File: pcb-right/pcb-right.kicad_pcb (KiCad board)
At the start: 2 copper layers, 143.4 x 118.9 mm, 91 parts, among them J1 Conn_01x02_Pin, J2 Conn_01x06_MountingPin, J3 Conn_01x04_Pin, SW1 SW_Push, SW2 Rotary_Encoder_Default, U1 XC6206PxxxMR, U2 STM32F401RCTx, Y1 12MHz

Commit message: moved daughter board to separate projects for left and right halves fixed layouts of daughter boards..
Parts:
- removed the R1 at (58.2, 82.7)
- removed R3: 1k, Resistor_SMD:R_0402_1005Metric
- C1, C10, C11, C12, C13, C2, C3, C4, C5, C6, C7, C8, C9: footprint Capacitor_SMD:C_0402_1005Metric -> Capacitor_SMD:C_0603_1608Metric
- R1: renamed from R5; footprint Resistor_SMD:R_0402_1005Metric -> Resistor_SMD:R_0603_1608Metric_Pad0.98x0.95mm_HandSolder
- R10, R11, R12, R13, R7, R8, R9: footprint Resistor_SMD:R_0402_1005Metric -> Resistor_SMD:R_0603_1608Metric_Pad0.98x0.95mm_HandSolder
- R2: renamed from R6; footprint Resistor_SMD:R_0402_1005Metric -> Resistor_SMD:R_0603_1608Metric_Pad0.98x0.95mm_HandSolder
- R4: renamed from R2; footprint Resistor_SMD:R_0402_1005Metric -> Resistor_SMD:R_0603_1608Metric_Pad0.98x0.95mm_HandSolder; moved to F.Cu
- R6: renamed from R4; footprint Resistor_SMD:R_0402_1005Metric -> Resistor_SMD:R_0603_1608Metric_Pad0.98x0.95mm_HandSolder; moved to F.Cu
- moved R4 18.4 mm to (62.3, 63.4), turned to -90 degrees
- moved R6 17.2 mm to (64.1, 63.4), turned to -90 degrees
- moved D29 9.23 mm to (84.9, 92.0), turned to 180 degrees
- moved R13 3.67 mm to (57.5, 86.2)
- moved R10 3.00 mm to (63.3, 90.9)
- moved R11 2.80 mm to (63.3, 95.0)
- moved J1 2.56 mm to (76.3, 86.6)
- moved R7 2.43 mm to (60.1, 86.2)
- moved C6 2.27 mm to (72.3, 81.5), turned to -90 degrees
- moved R8 2.22 mm to (60.8, 90.9)
- moved C13 2.19 mm to (69.3, 89.8)
- moved C12 2.06 mm to (72.1, 86.4)
- moved R9 1.95 mm to (60.8, 95.0)
- moved Y1 1.72 mm to (69.3, 86.4)
- moved R12 1.50 mm to (66.5, 86.4)
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- renumbered D26 to D25, D27 to D26, D28 to D27, D29 to D28, D30 to D29, MX26 to MX25, MX27 to MX26, MX28 to MX27, MX29 to MX28
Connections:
- R4 pad 2: Net-(U2-PA2) -> /UART_TX
- R6 pad 2: Net-(U2-PA3) -> /UART_RX
- U2 pad 16: Net-(U2-PA2) -> unconnected-(U2-PA2-Pad16)
- U2 pad 17: Net-(U2-PA3) -> unconnected-(U2-PA3-Pad17)
- U2 pad 37: unconnected-(U2-PC6-Pad37) -> /UART_TX
- U2 pad 38: unconnected-(U2-PC7-Pad38) -> /UART_RX
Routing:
- net /SPLIT_TX: track 38.9 -> 8.24 mm, vias 1 -> 0
- net /SPLIT_RX: track 35.3 -> 6.73 mm, vias 1 -> 0
- net /ROW4: track 154.6 -> 144.0 mm
- net /ENC_SW_2: track 3.02 -> 11.6 mm
- net +3V3: track 102.0 -> 107.3 mm
- net /UART_RX: track 0.00 -> 4.36 mm, vias 0 -> 1
- net /UART_TX: track 0.00 -> 4.36 mm, vias 0 -> 1
- net Net-(U2-PA2): track 4.20 -> 0.00 mm
- net /HANDEDNESS: track 8.20 -> 12.2 mm
- net Net-(U2-PA3): track 3.91 -> 0.00 mm
- net /ENC_B: track 13.6 -> 10.8 mm
- net /BOOTSEL: track 11.5 -> 14.2 mm
- net /ENC_A: track 14.0 -> 11.7 mm
- net /XIN: track 7.00 -> 9.21 mm
- net GND: track 19.9 -> 21.8 mm, vias 10 -> 53
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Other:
- outline, holes or cut-outs redrawn

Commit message: quick save
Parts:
- removed R1, R2: 27, Resistor_SMD:R_0603_1608Metric_Pad0.98x0.95mm_HandSolder
- removed R10, R8: 5.1k, Resistor_SMD:R_0603_1608Metric_Pad0.98x0.95mm_HandSolder
- removed R12: 1k, Resistor_SMD:R_0603_1608Metric_Pad0.98x0.95mm_HandSolder
- added C14: 100n, Capacitor_SMD:C_0603_1608Metric, B.Cu at (71.7, 45.8)
- added D30: ~, lib-zegonix:SK6812MINI-E_3.2x2.8_reverse_mount, F.Cu at (64.5, 45.8)
- added R14: 10k, Resistor_SMD:R_0603_1608Metric, B.Cu at (75.5, 111.4)
- added R15: 10k, Resistor_SMD:R_0603_1608Metric, B.Cu at (73.1, 63.5)
- C10, R4, R6, SW1: moved to B.Cu
- C12, C13: value 22p -> 12p
- J2: footprint Connector_JST:JST_SHL_SM06B-SHLS-TF_1x06-1MP_P1.00mm_Horizontal -> Connector_JST:JST_SH_SM06B-SRSS-TB_1x06-1MP_P1.00mm_Horizontal; moved to B.Cu
- R11, R9: value 5.1k -> 10K
- Y1: value 12MHz -> 8MHz
- moved SW1 66.6 mm to (58.1, 116.2)
- moved C10 53.4 mm to (59.2, 109.8), turned to 180 degrees
- moved J1 23.9 mm to (71.7, 110.1)
- moved J3 4.92 mm to (67.7, 39.0)
- moved J2 3.63 mm to (55.8, 56.6)
- moved Y1 0.62 mm to (68.8, 86.1)
- moved C13 0.49 mm to (68.8, 89.8)
- moved C12 0.38 mm to (72.1, 86.1)
- moved R4 0.25 mm to (62.0, 63.4)
- moved R6 0.25 mm to (64.3, 63.4)
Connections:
- C13 pad 2: Net-(C13-Pad2) -> /XOUT
- J1 pad 1: /BOOTSEL -> +3V3
- J1 pad 2: GND -> /BOOT0
- R11 pad 1: Net-(R10-Pad2) -> /ENC_B
- R9 pad 2: Net-(R8-Pad1) -> /ENC_A
- U2 pad 28: unconnected-(U2-PB2-Pad28) -> /BOOT1
- U2 pad 34: unconnected-(U2-PB13-Pad34) -> /IND_LED
- U2 pad 44: Net-(U2-PA11) -> /USB_D-
- U2 pad 45: Net-(U2-PA12) -> /USB_D+
- U2 pad 60: /BOOTSEL -> /BOOT0
- Y1 pad 1: Net-(C13-Pad2) -> /XOUT
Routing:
- net /BOOT0: track 0.00 -> 45.4 mm, vias 0 -> 2
- net +3V3: track 107.3 -> 148.0 mm, vias 3 -> 4
- net /IND_LED: track 0.00 -> 22.9 mm, vias 0 -> 2
- net /BOOT1: track 0.00 -> 18.9 mm, vias 0 -> 2
- net /BOOTSEL: track 14.2 -> 0.00 mm, vias 1 -> 0
- net /SWCLK: track 28.9 -> 37.2 mm
- net /USB_D-: track 13.1 -> 21.0 mm, vias 1 -> 0
- net +5V: track 6.45 -> 14.3 mm, vias 1 -> 0
- net /nRESET: track 36.9 -> 44.6 mm, vias 1 -> 2
- net /USB_D+: track 14.4 -> 22.0 mm, vias 1 -> 0
- net /SPLIT_TX: track 8.24 -> 13.5 mm
- net /SPLIT_RX: track 6.73 -> 11.8 mm
- net /XOUT: track 5.97 -> 10.7 mm
- net Net-(C13-Pad2): track 4.31 -> 0.00 mm
- net /ENC_B: track 10.8 -> 15.0 mm
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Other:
- outline, holes or cut-outs redrawn

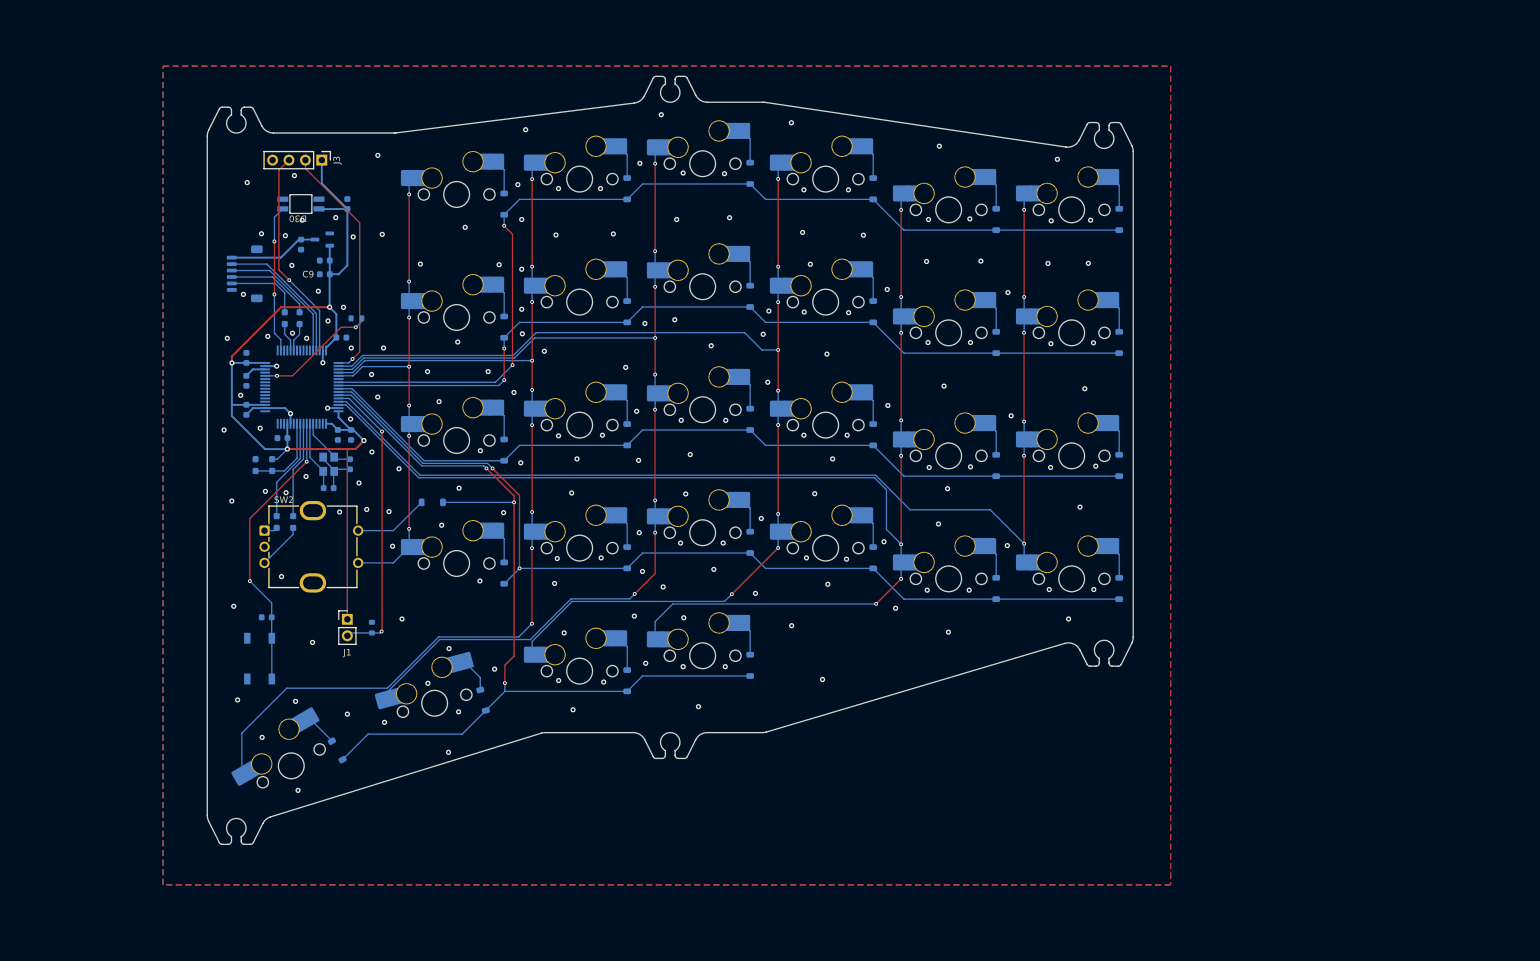
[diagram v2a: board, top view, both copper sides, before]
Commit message: finalised first version of pcbs for prototype order added openscad file for the left halfs case
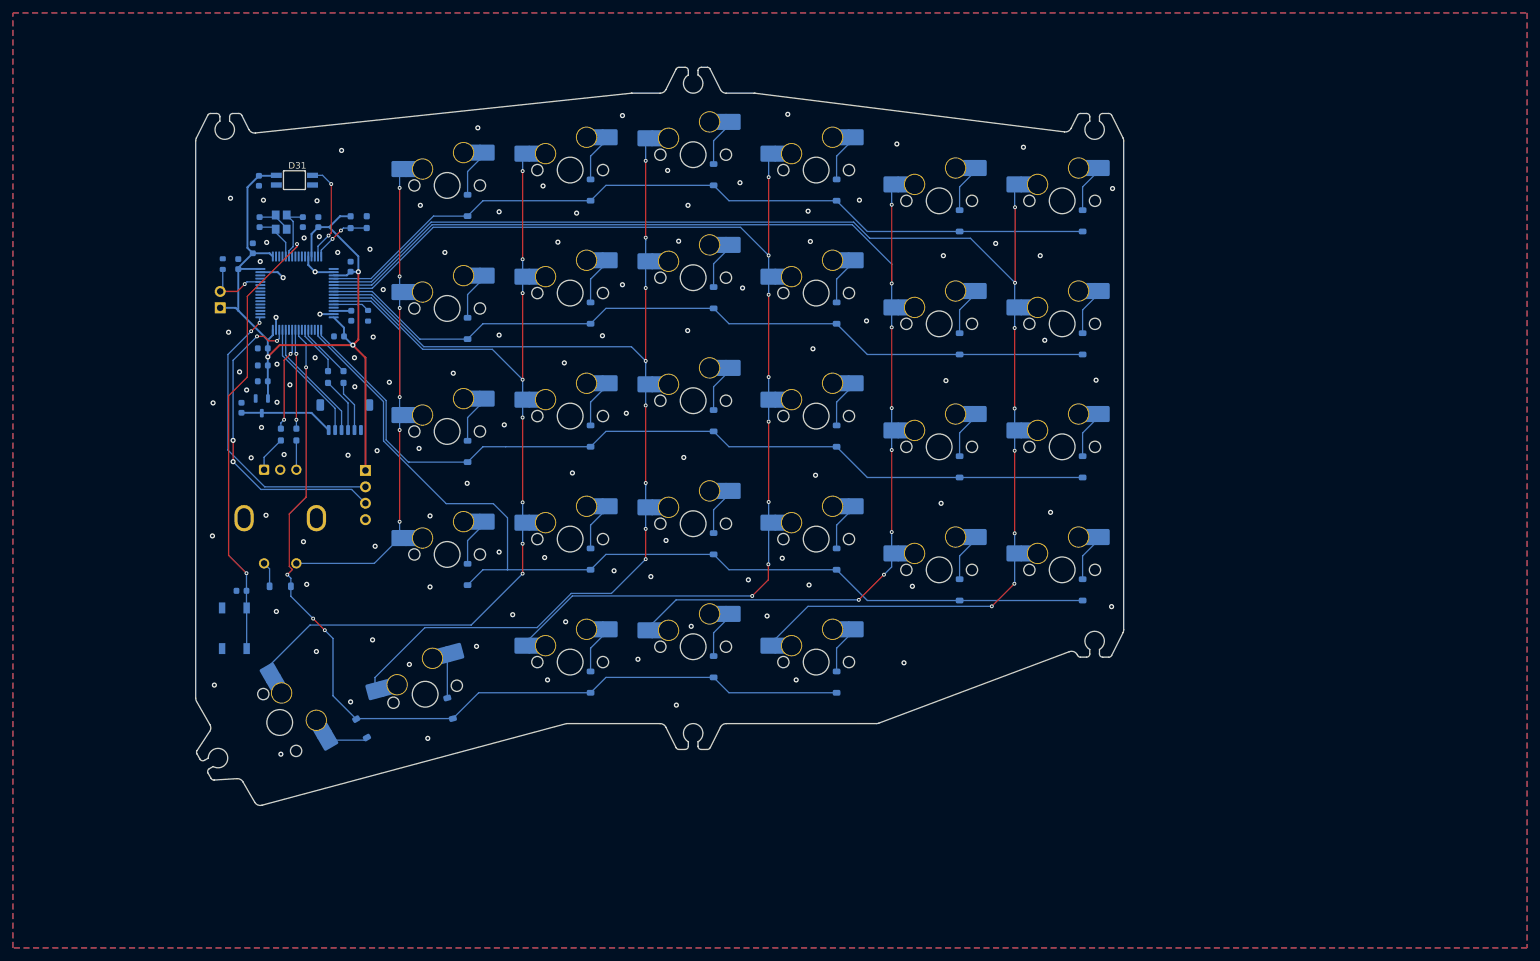
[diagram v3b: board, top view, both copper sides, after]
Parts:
- removed R11: 10K, Resistor_SMD:R_0603_1608Metric_Pad0.98x0.95mm_HandSolder
- removed R13: 5.1k, Resistor_SMD:R_0603_1608Metric_Pad0.98x0.95mm_HandSolder
- removed R14, R15: 10k, Resistor_SMD:R_0603_1608Metric
- added D31: ~, lib-zegonix:SK6812MINI-E_3.2x2.8_reverse_mount, F.Cu at (63.5, 42.1)
- added MX29: MX_SW_HS, PCM_marbastlib-mx:SW_MX_HS_1u, B.Cu at (61.2, 126.1)
- added R1: 10k, Resistor_SMD:R_0603_1608Metric, B.Cu at (52.4, 55.1)
- added R10: 10k, Resistor_SMD:R_0603_1608Metric_Pad0.98x0.95mm_HandSolder, B.Cu at (74.7, 48.6)
- added R2: 10k, Resistor_SMD:R_0603_1608Metric, B.Cu at (74.9, 63.1)
- added R8: 10K, Resistor_SMD:R_0603_1608Metric_Pad0.98x0.95mm_HandSolder, B.Cu at (61.4, 81.5)
- C13: value 12p -> 100n
- C14: value 100n -> 12p
- D30: value ~ -> D_Small; footprint lib-zegonix:SK6812MINI-E_3.2x2.8_reverse_mount -> Diode_SMD:D_SOD-123; moved to B.Cu
- J1: value Conn_01x02_Pin -> Conn_01x04_Pin; footprint Connector_PinHeader_2.54mm:PinHeader_1x02_P2.54mm_Vertical -> Connector_PinHeader_2.54mm:PinHeader_1x04_P2.54mm_Vertical; moved to B.Cu
- J2: value Conn_01x06_MountingPin -> Conn_01x02_Pin; footprint Connector_JST:JST_SH_SM06B-SRSS-TB_1x06-1MP_P1.00mm_Horizontal -> Connector_PinHeader_2.54mm:PinHeader_1x02_P2.54mm_Vertical
- J3: value Conn_01x04_Pin -> Conn_01x06_MountingPin; footprint Connector_PinHeader_2.54mm:PinHeader_1x04_P2.54mm_Vertical -> Connector_JST:JST_SH_SM06B-SRSS-TB_1x06-1MP_P1.00mm_Horizontal; moved to B.Cu
- R7: value 5.1k -> 10k
- SW2: moved to B.Cu
- moved D30 59.3 mm to (61.3, 105.0)
- moved C13 48.8 mm to (58.0, 42.2), turned to -90 degrees
- moved C12 40.0 mm to (58.1, 48.6), turned to -90 degrees
- moved J3 40.0 mm to (71.3, 78.8), turned to 0 degrees
- moved R7 39.5 mm to (72.2, 48.6)
- moved Y1 38.2 mm to (61.5, 48.6), turned to -90 degrees
- moved D29 36.7 mm to (73.9, 127.0), turned to -60 degrees
- moved C4 31.8 mm to (57.1, 52.6), turned to 90 degrees
- moved U1 27.4 mm to (58.5, 77.0), turned to -90 degrees
- moved C8 26.9 mm to (55.3, 77.3), turned to 90 degrees
- moved C6 26.1 mm to (72.2, 55.5), turned to 90 degrees
- moved C7 23.8 mm to (67.2, 48.6)
- moved MX28 23.5 mm to (83.7, 121.7), turned to -165 degrees
- moved J1 23.2 mm to (74.5, 87.0), turned to 180 degrees
- moved MX27 21.9 mm to (106.2, 116.7), turned to 180 degrees
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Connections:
- C13 pad 1: GND -> +3V3
- C13 pad 2: /XOUT -> GND
- C14 pad 1: +3V3 -> GND
- C14 pad 2: GND -> /XOUT
- D29 pad 2: /ENC_SW_2 -> Net-(D29-A)
- D30 pad 1: +3V3 -> /ROW4
- D30 pad 2: unconnected-(D30-DOUT-Pad2) -> /ENC_SW_2
- J1 pad 2: /BOOT0 -> /SWCLK
- J2 pad 1: +5V -> +3V3
- J2 pad 2: /USB_D+ -> /BOOT0
- J3 pad 1: +3V3 -> +5V
- J3 pad 2: /SWCLK -> /USB_D+
- J3 pad 3: /SWDIO -> /USB_D-
- J3 pad 4: GND -> /SPLIT_TX
- MX25 pad 1: /COL1 -> /COL0
- MX26 pad 1: /COL2 -> /COL1
- MX27 pad 1: /COL3 -> /COL2
- MX28 pad 1: /COL4 -> /COL3
- R9 pad 1: Net-(R9-Pad1) -> /ENC_B
- R9 pad 2: /ENC_A -> Net-(R9-Pad2)
- SW2 pad A: Net-(R9-Pad1) -> Net-(R8-Pad1)
- SW2 pad B: Net-(R11-Pad2) -> Net-(R9-Pad2)
- U2 pad 10: /HANDEDNESS -> unconnected-(U2-PC2-Pad10)
- U2 pad 15: unconnected-(U2-PA1-Pad15) -> /IND_LED
- U2 pad 16: unconnected-(U2-PA2-Pad16) -> /HANDEDNESS
- U2 pad 20: unconnected-(U2-PA4-Pad20) -> /ROW0
- U2 pad 21: unconnected-(U2-PA5-Pad21) -> /COL0
- U2 pad 22: unconnected-(U2-PA6-Pad22) -> /COL1
- U2 pad 23: unconnected-(U2-PA7-Pad23) -> /COL2
- U2 pad 24: unconnected-(U2-PC4-Pad24) -> /ROW1
- U2 pad 25: unconnected-(U2-PC5-Pad25) -> /COL3
- U2 pad 26: unconnected-(U2-PB0-Pad26) -> /COL4
- U2 pad 27: unconnected-(U2-PB1-Pad27) -> /COL5
- U2 pad 33: unconnected-(U2-PB12-Pad33) -> /ROW2
- U2 pad 34: /IND_LED -> /ROW3
- U2 pad 40: unconnected-(U2-PC9-Pad40) -> /ROW4
- U2 pad 41: unconnected-(U2-PA8-Pad41) -> /ENC_B
- U2 pad 42: unconnected-(U2-PA9-Pad42) -> /ENC_A
- U2 pad 50: /COL2 -> unconnected-(U2-PA15-Pad50)
- U2 pad 51: /COL3 -> unconnected-(U2-PC10-Pad51)
- U2 pad 52: /COL4 -> unconnected-(U2-PC11-Pad52)
- U2 pad 53: /COL5 -> unconnected-(U2-PC12-Pad53)
- U2 pad 55: /ROW0 -> unconnected-(U2-PB3-Pad55)
- U2 pad 56: /ROW1 -> unconnected-(U2-PB4-Pad56)
- U2 pad 57: /ROW2 -> unconnected-(U2-PB5-Pad57)
- U2 pad 58: /ROW3 -> unconnected-(U2-PB6-Pad58)
- U2 pad 59: /ROW4 -> unconnected-(U2-PB7-Pad59)
- U2 pad 61: /COL0 -> unconnected-(U2-PB8-Pad61)
- U2 pad 62: /COL1 -> unconnected-(U2-PB9-Pad62)
- U2 pad 8: /ENC_B -> unconnected-(U2-PC0-Pad8)
- U2 pad 9: /ENC_A -> unconnected-(U2-PC1-Pad9)
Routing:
- net /COL0: track 172.5 -> 217.2 mm, vias 6 -> 8
- net /BOOT0: track 45.4 -> 10.4 mm, vias 2 -> 1
- net /ROW0: track 152.1 -> 124.9 mm, vias 2 -> 0
- net /nRESET: track 44.6 -> 70.4 mm
- net +3V3: track 148.0 -> 127.6 mm, vias 4 -> 3
- net /COL5: track 77.6 -> 97.2 mm, vias 7 -> 6
- net /SWDIO: track 32.7 -> 49.4 mm, vias 1 -> 4
- net /COL4: track 160.7 -> 145.8 mm, vias 9 -> 8
- net /BOOT1: track 18.9 -> 5.71 mm, vias 2 -> 0
- net /SWCLK: track 37.2 -> 46.3 mm, vias 1 -> 2
- net /ROW1: track 132.8 -> 124.0 mm, vias 2 -> 0
- net /ENC_SW_2: track 11.6 -> 3.90 mm
- net /ROW3: track 146.2 -> 153.8 mm, vias 2 -> 0
- net /IND_LED: track 22.9 -> 15.5 mm
- net Net-(R11-Pad2): track 7.26 -> 0.00 mm
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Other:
- board size 143.4 x 118.9 mm -> 143.7 x 114.3 mm
